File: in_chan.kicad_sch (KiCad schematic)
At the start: 17 parts, among them U8 MAX31910AUI+

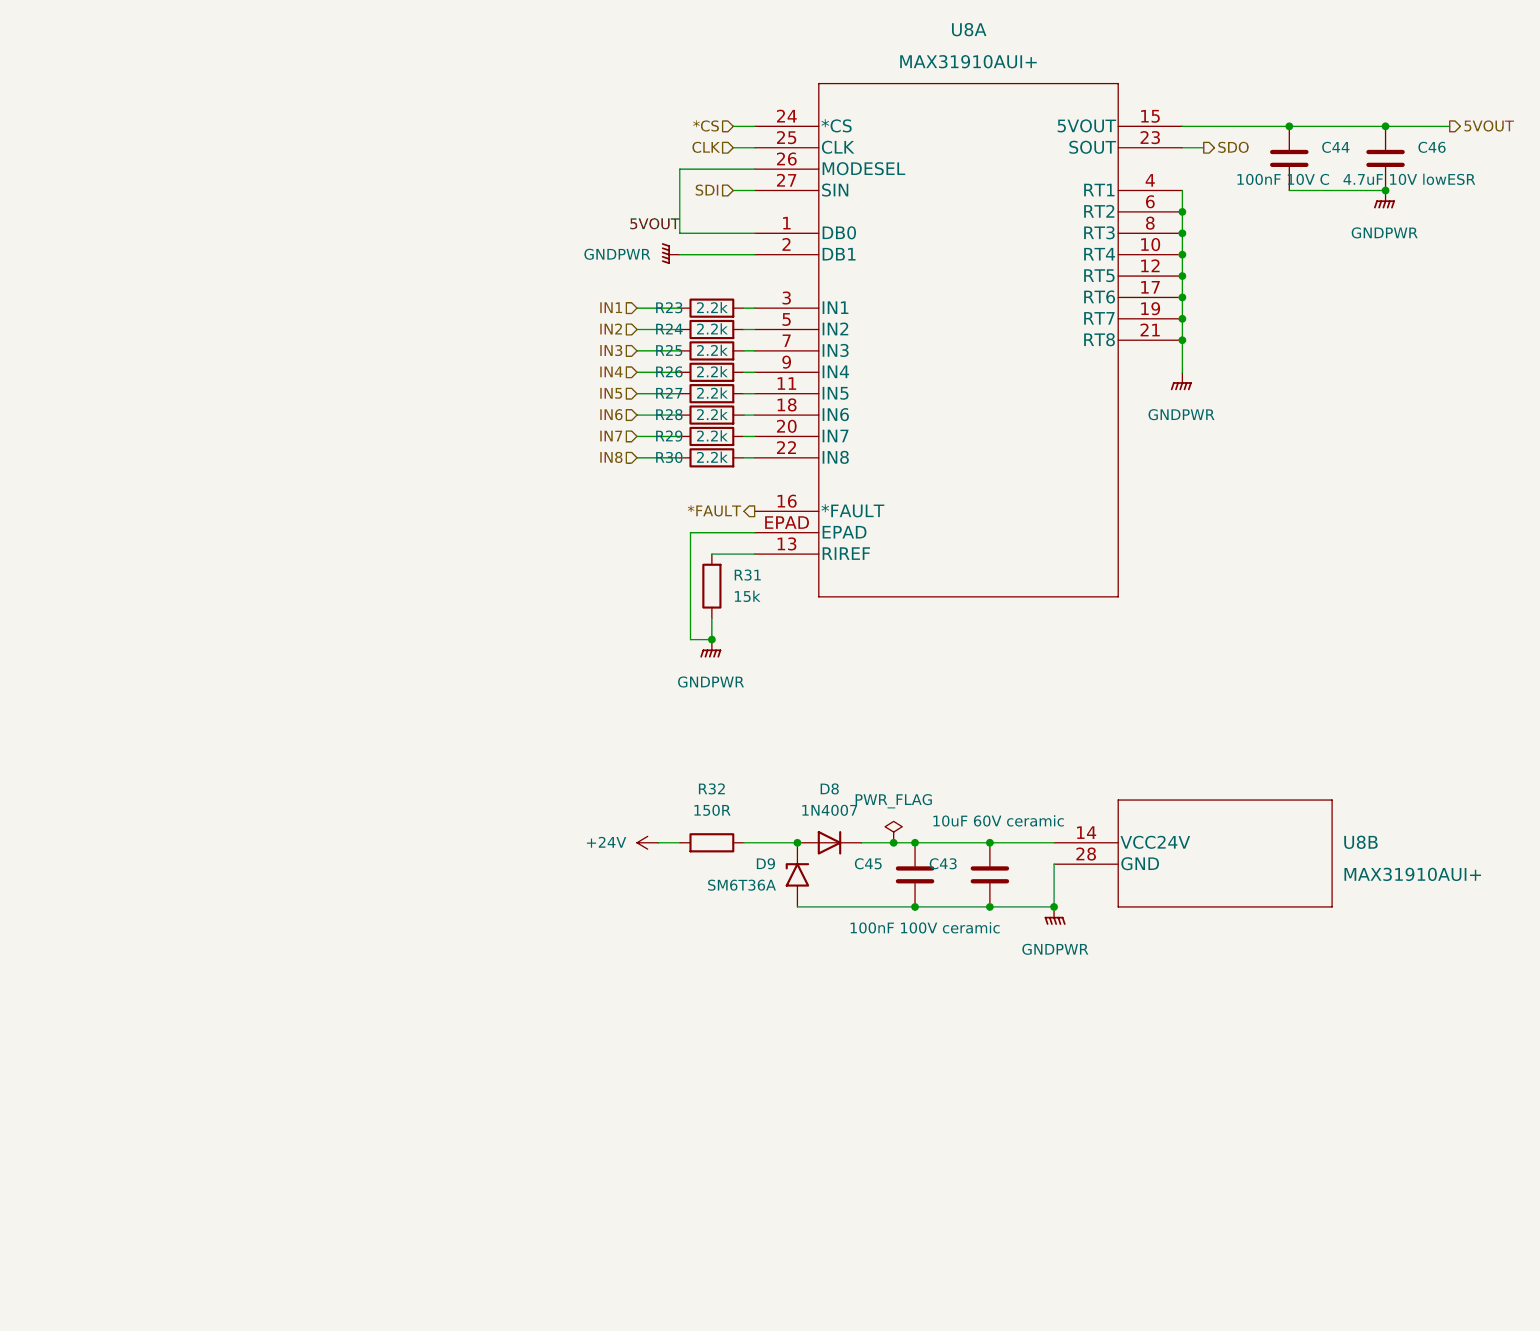
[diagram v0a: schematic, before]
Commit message: Common power stage for field IO
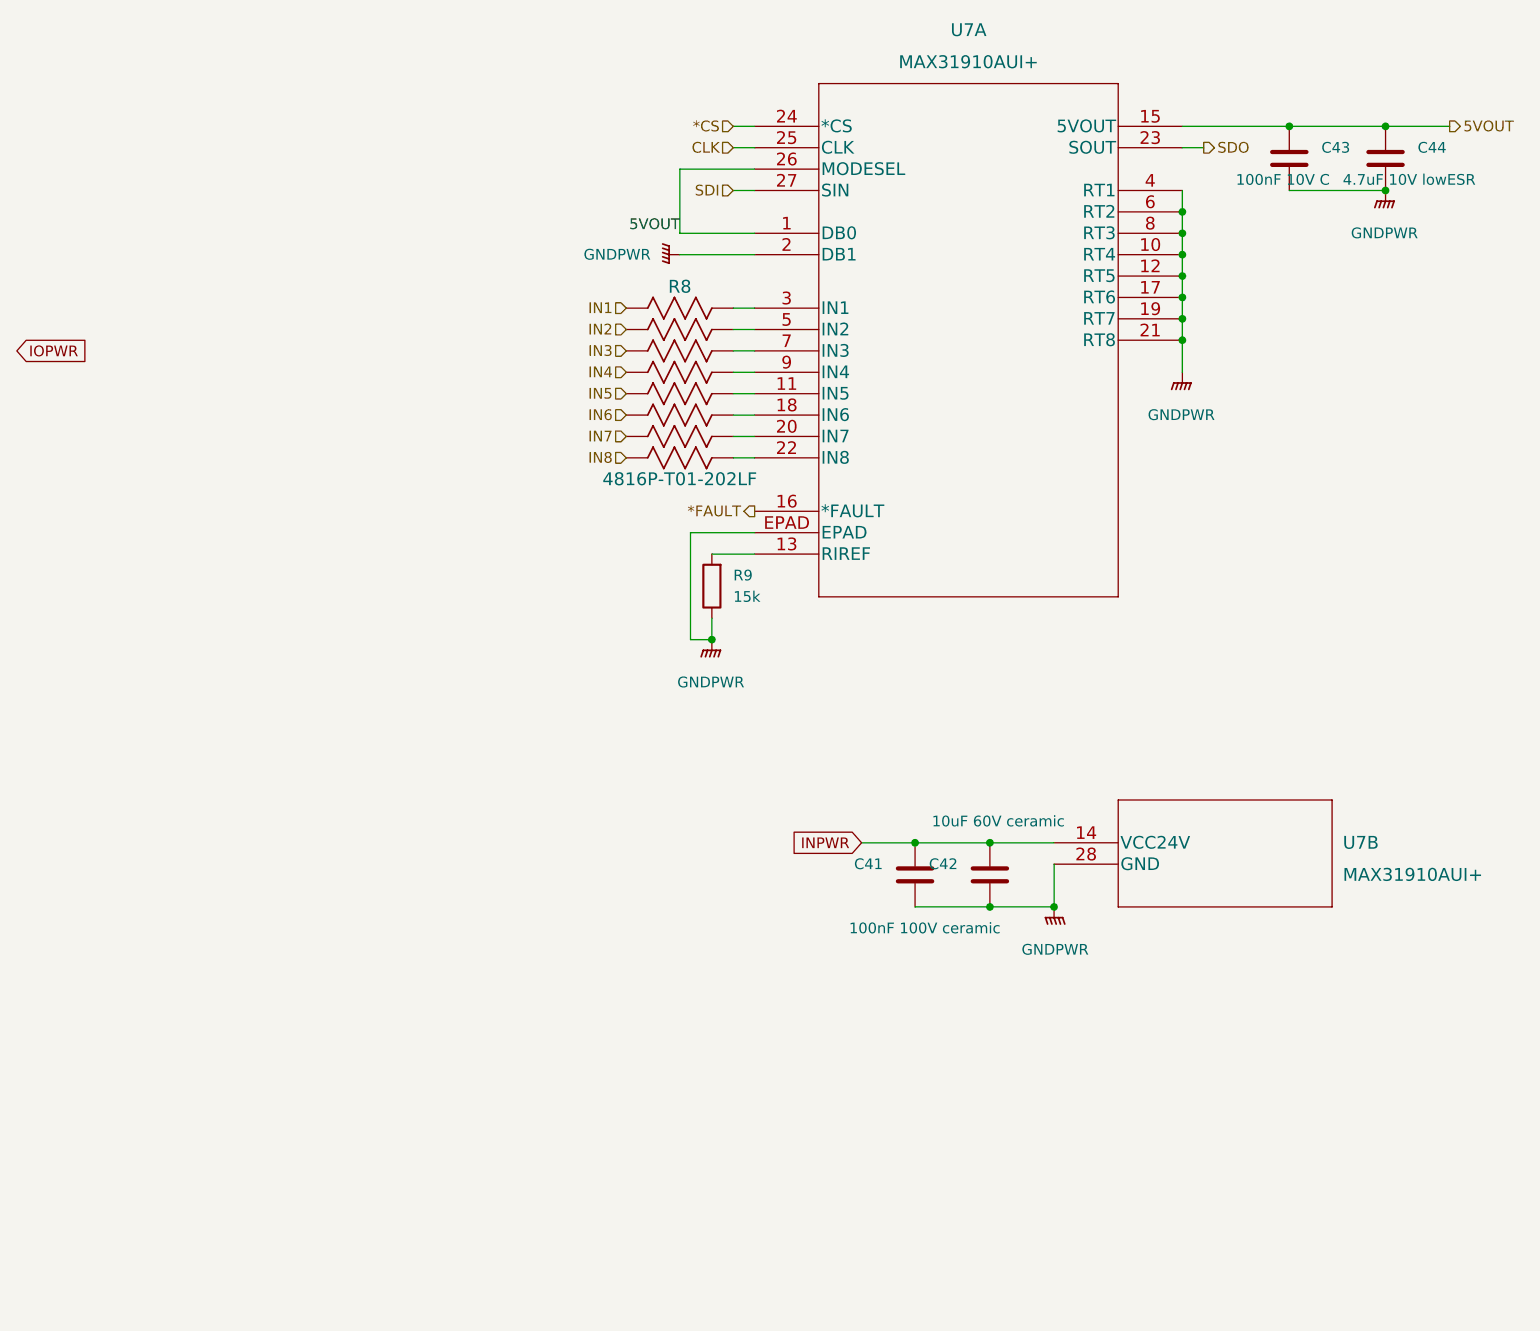
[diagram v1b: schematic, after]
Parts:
- removed D8: 1N4007, Diode_SMD:D_MELF, symbol Diode:SM4007
- removed D9: SM6T36A, Diode_SMD:D_SMB, symbol Diode:SM6T36A
- removed R23, R24, R25, R26, R27, R28, R29, R30: 2.2k, Resistor_SMD:R_0402_1005Metric, symbol Device:R
- removed R32: 150R, Resistor_SMD:R_0805_2012Metric, symbol Device:R
- added R8: 4816P-T01-202LF, Maxim industrial IO:4816P, symbol Num-IO:4816P-T01-103LF
- renumbered C45 to C41, C43 to C42, C44 to C43, C46 to C44, R31 to R9, U8 to U7
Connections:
- net IN1: now also R8.1
- net IN2: now also R8.2
- net IN3: now also R8.3
- net IN4: now also R8.4
- net IN5: now also R8.5
- net IN6: now also R8.6
- net IN7: now also R8.7
- net IN8: now also R8.8
- net at U7.9 (IN4): now also R8.13
- net at U7.18 (IN6): now also R8.11
- net at U7.22 (IN8): now also R8.9
- net at U7.5 (IN2): now also R8.15
- net at U7.20 (IN7): now also R8.10
- net INPWR: now reaches C41.1, C42.1, U7.14 (VCC24V)
- net at U7.11 (IN5): now also R8.12
- net at U7.3 (IN1): now also R8.16
- net at U7.7 (IN3): now also R8.14

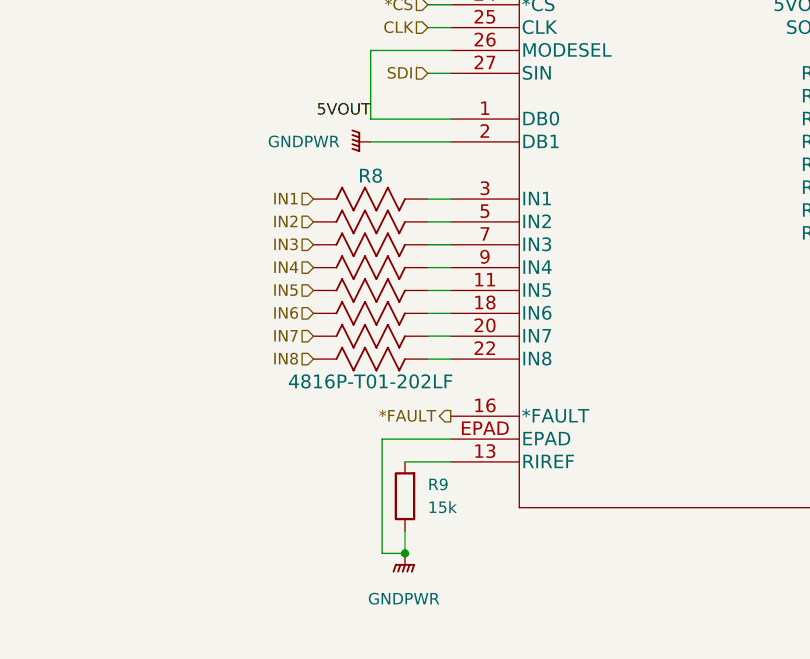
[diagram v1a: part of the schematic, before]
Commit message: Further simplifying the schematics
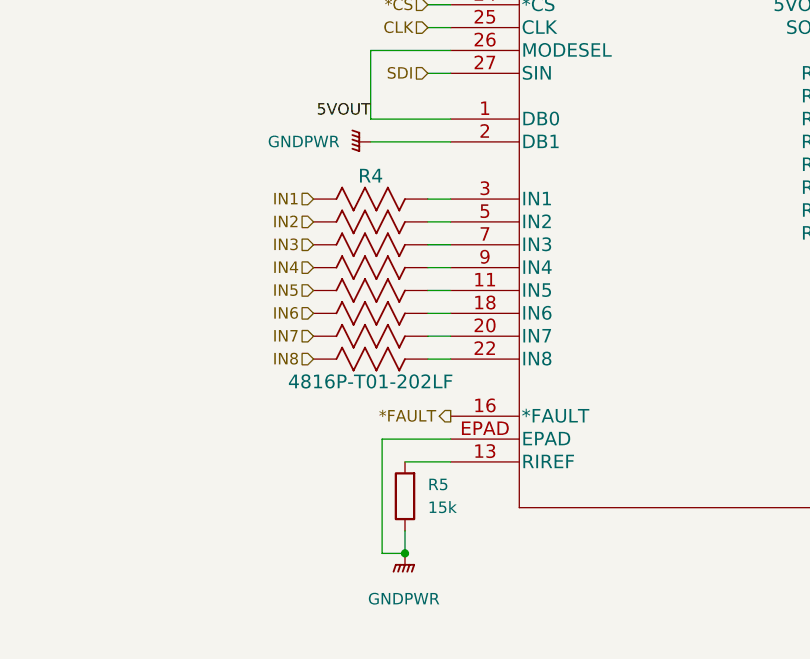
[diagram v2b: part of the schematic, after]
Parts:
- renumbered R8 to R4, R9 to R5
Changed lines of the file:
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@@
   (symbol (lib_id "Device:R") (at 163.83 113.03 180) (unit 1)
     (in_bom yes) (on_board yes)
-    (property "Reference" "R9" (id 0) (at 166.37 111.76 0)
+    (property "Reference" "R5" (id 0) (at 166.37 111.76 0)
       (effects (font (size 1.27 1.27)) (justify right))
     )
@@
   (symbol (lib_id "Num-IO:4816P-T01-103LF") (at 153.67 80.01 0) (unit 1)
     (in_bom yes) (on_board yes)
-    (property "Reference" "R8" (id 0) (at 160.02 77.47 0)
+    (property "Reference" "R4" (id 0) (at 160.02 77.47 0)
       (effects (font (size 1.524 1.524)))
     )

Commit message: fix DRC errors
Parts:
- R9: renamed from R5; Power (none) -> 1/8W
- renumbered C41 to C37, C42 to C38, C43 to C39, C44 to C40, R4 to R8, U7 to U6
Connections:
- net GNDPWR: now also U6.25 (CLK), U6.27 (SIN); no longer U6.28 (GND)
- net INPWR: now also U6.24 (*CS); no longer U6.14 (VCC24V)

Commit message: routing stuff
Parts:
- renumbered C37 to C45, C38 to C46, C39 to C47, C40 to C48, R8 to R10, R9 to R11, U6 to U8
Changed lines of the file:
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@@
   (symbol (lib_id "power:GNDPWR") (at 163.83 119.38 0)
     (in_bom yes) (on_board yes) (fields_autoplaced)
-    (property "Reference" "#PWR036" (id 0) (at 163.83 124.46 0)
+    (property "Reference" "#PWR051" (id 0) (at 163.83 124.46 0)
       (effects (font (size 1.27 1.27)) hide)
     )
@@
   (symbol (lib_id "Device:R") (at 163.83 113.03 180)
     (in_bom yes) (on_board yes)
-    (property "Reference" "R9" (id 0) (at 166.37 111.76 0)
+    (property "Reference" "R11" (id 0) (at 166.37 111.76 0)
       (effects (font (size 1.27 1.27)) (justify right))
     )
@@
   (symbol (lib_id "power:GNDPWR") (at 204.47 151.13 0) (mirror y)
     (in_bom yes) (on_board yes) (fields_autoplaced)
-    (property "Reference" "#PWR037" (id 0) (at 204.47 156.21 0)
+    (property "Reference" "#PWR052" (id 0) (at 204.47 156.21 0)
       (effects (font (size 1.27 1.27)) hide)
     )
@@
   (symbol (lib_id "power:GNDPWR") (at 243.84 66.04 0)
     (in_bom yes) (on_board yes) (fields_autoplaced)
-    (property "Reference" "#PWR039" (id 0) (at 243.84 71.12 0)
+    (property "Reference" "#PWR054" (id 0) (at 243.84 71.12 0)
       (effects (font (size 1.27 1.27)) hide)
     )
@@
   (symbol (lib_id "Device:C") (at 243.84 62.23 0)
     (in_bom yes) (on_board yes)
-    (property "Reference" "C40" (id 0) (at 247.65 60.9599 0)
+    (property "Reference" "C48" (id 0) (at 247.65 60.9599 0)
       (effects (font (size 1.27 1.27)) (justify left))
     )
@@
   (symbol (lib_id "Maxim industrial IO:MAX31910AUI+") (at 204.47 143.51 0)
     (in_bom yes) (on_board yes) (fields_autoplaced)
-    (property "Reference" "U6" (id 0) (at 238.76 143.51 0)
+    (property "Reference" "U8" (id 0) (at 238.76 143.51 0)
       (effects (font (size 1.524 1.524)) (justify left))
     )
@@
       (effects (font (size 1.524 1.524)))
     )
-    (pin "14")
-    (pin "28")
+    (pin "1")
+    (pin "10")
+    (pin "11")
+    (pin "12")
+    (pin "13")
+    (pin "15")
+    (pin "16")
+    (pin "17")
+    (pin "18")
+    (pin "19")
+    (pin "2")
+    (pin "20")
+    (pin "21")
+    (pin "22")
+    (pin "23")
+    (pin "24")
+    (pin "25")
+    (pin "26")
+    (pin "27")
+    (pin "3")
+    (pin "4")
+    (pin "5")
+    (pin "6")
+    (pin "7")
+    (pin "8")
+    (pin "9")
+    (pin "EPAD")
   )
   (symbol (lib_id "Device:C") (at 187.96 147.32 0) (mirror y)
     (in_bom yes) (on_board yes)
-    (property "Reference" "C37" (id 0) (at 184.15 146.0499 0)
+    (property "Reference" "C45" (id 0) (at 184.15 146.0499 0)
       (effects (font (size 1.27 1.27)) (justify left))
     )
@@
   (symbol (lib_id "power:GNDPWR") (at 219.71 87.63 0)
     (in_bom yes) (on_board yes) (fields_autoplaced)
-    (property "Reference" "#PWR038" (id 0) (at 219.71 92.71 0)
+    (property "Reference" "#PWR053" (id 0) (at 219.71 92.71 0)
       (effects (font (size 1.27 1.27)) hide)
     )
@@
   (symbol (lib_id "Device:C") (at 232.41 62.23 0)
     (in_bom yes) (on_board yes)
-    (property "Reference" "C39" (id 0) (at 236.22 60.9599 0)
+    (property "Reference" "C47" (id 0) (at 236.22 60.9599 0)
       (effects (font (size 1.27 1.27)) (justify left))
     )
@@
   (symbol (lib_id "power:GNDPWR") (at 160.02 73.66 270)
     (in_bom yes) (on_board yes)
-    (property "Reference" "#PWR035" (id 0) (at 154.94 73.66 0)
+    (property "Reference" "#PWR050" (id 0) (at 154.94 73.66 0)
       (effects (font (size 1.27 1.27)) hide)
     )
@@
   (symbol (lib_id "Device:C") (at 196.85 147.32 0) (mirror y)
     (in_bom yes) (on_board yes)
-    (property "Reference" "C38" (id 0) (at 193.04 146.0499 0)
+    (property "Reference" "C46" (id 0) (at 193.04 146.0499 0)
       (effects (font (size 1.27 1.27)) (justify left))
     )
@@
   (symbol (lib_id "Num-IO:4816P-T01-103LF") (at 153.67 80.01 0)
     (in_bom yes) (on_board yes)
-    (property "Reference" "R8" (id 0) (at 160.02 77.47 0)
+    (property "Reference" "R10" (id 0) (at 160.02 77.47 0)
       (effects (font (size 1.524 1.524)))
     )
@@
   (symbol (lib_id "Maxim industrial IO:MAX31910AUI+") (at 168.91 58.42 0)
     (in_bom yes) (on_board yes) (fields_autoplaced)
-    (property "Reference" "U6" (id 0) (at 194.31 46.99 0)
-      (effects (font (size 1.524 1.524)))
-    )
+    (property "Reference" "U8" (id 0) (at 194.31 46.99 0)
+      (effects (font (size 1.524 1.524)))
+    )
